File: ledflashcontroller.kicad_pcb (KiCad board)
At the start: 2 copper layers, 100 x 100 mm, 68 parts, among them J1 Conn_02x08_Odd_Even, J2 CONN_01X02, J3 CONN_01X02, K1 LDD-1000H, K2 LDD-1000H, P1 V_DIM1, P10 BNC, P11 BNC, P12 BNC, P2 V_DIM2, P3 V_OUT, P4 V_IN, P5 I2C_HEADER, P6 GPIO_HEADER, P7 BNC, P8 BNC, P9 BNC, Q1 IRLML6244, Q2 IRFB3256, U1 Teensy3.6, U10 DMC2700, U2 ISO1540, U3 DMC2700, U4 DMC2700, U5 ISO1540, U6 DMC2700, U7 DMC2700, U8 ISO1540, U9 DMC2700

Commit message: Fixed some annotations and footprints
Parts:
- removed the P6 at (-56.7, 70.3)
- added P3: GPIO_HEADER, Pin_Headers:Pin_Header_Straight_1x06_Pitch2.54mm, F.Cu at (-40.1, 70.3)
- J1: footprint Pin_Headers:Pin_Header_Straight_2x08_Pitch1.00mm -> Pin_Headers:Pin_Header_Straight_2x08_Pitch2.54mm_SMD
- P10, P11, P12, P7, P8, P9: footprint Connectors_TE-Connectivity:BNC_Socket_TYCO-AMP_LargePads -> lib_fp:BNC_Socket_RSpro_LargePads
- renumbered P4 to P1, P5 to P2, P1 to P4, P2 to P5, P3 to P6, R8 to R1, R14 to R12, R12 to R13, R13 to R14, R17 to R15, R15 to R16, R16 to R17, R9 to R2, R22 to R20, R20 to R21, R21 to R22, R25 to R23, R23 to R24, R24 to R25, R30 to R28, R28 to R29, R7 to R3, R29 to R30, R33 to R31, R31 to R32, R32 to R33, R2 to R4, R3 to R5, R1 to R6, R4 to R7, R6 to R8, R5 to R9
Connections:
- U1 pad 23: (no net) -> /SCK1

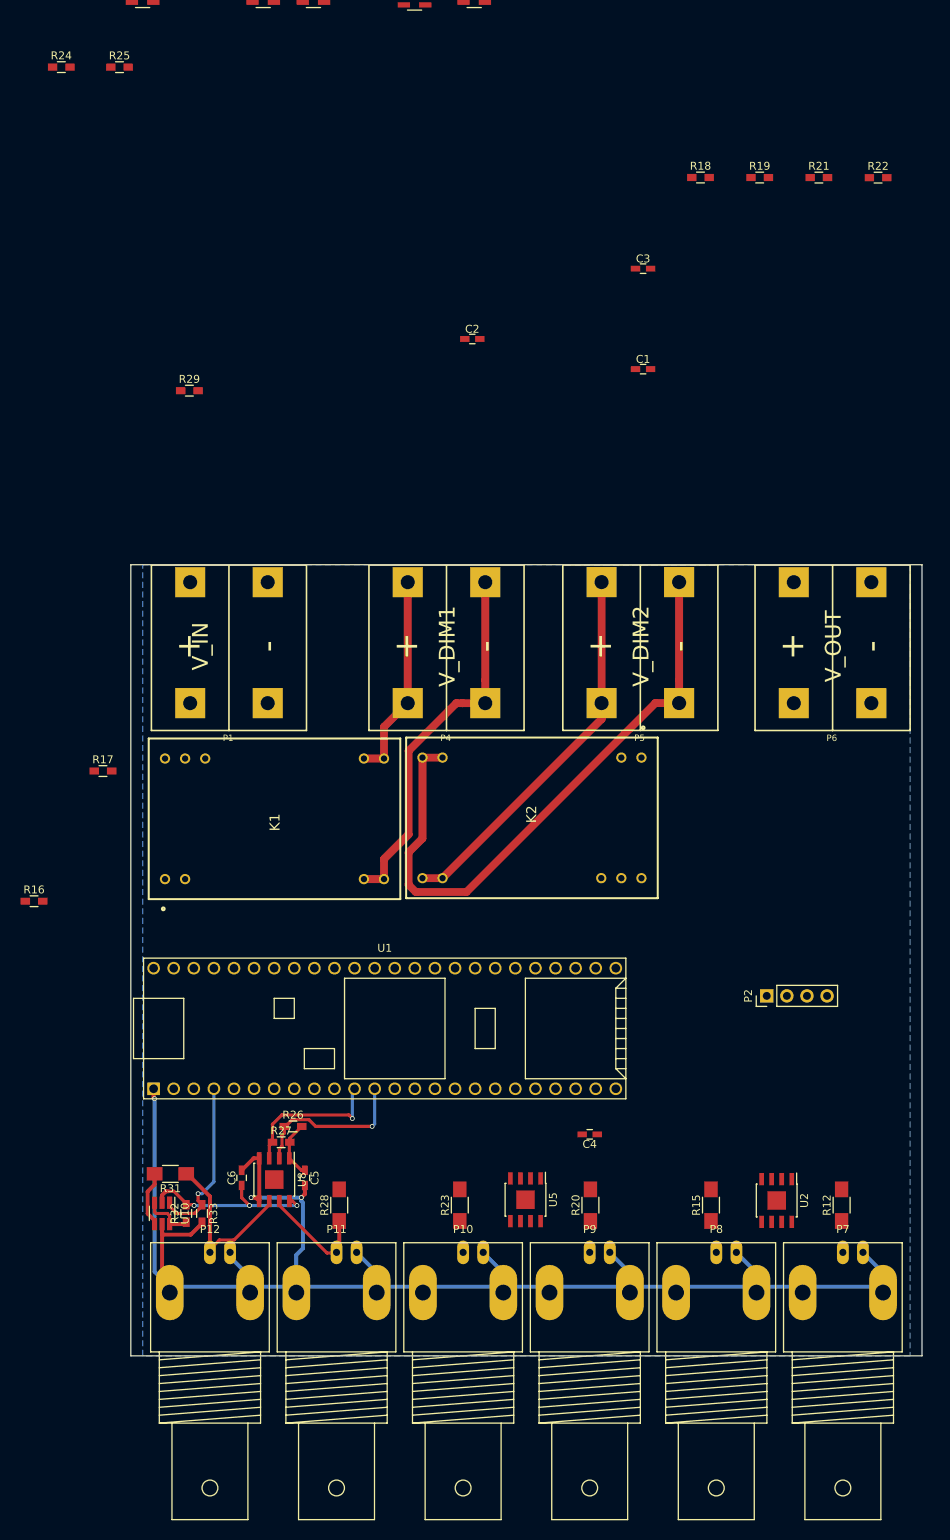
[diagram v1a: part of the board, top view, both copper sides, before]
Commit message: Restructured existing connections and aligned everythink to grid
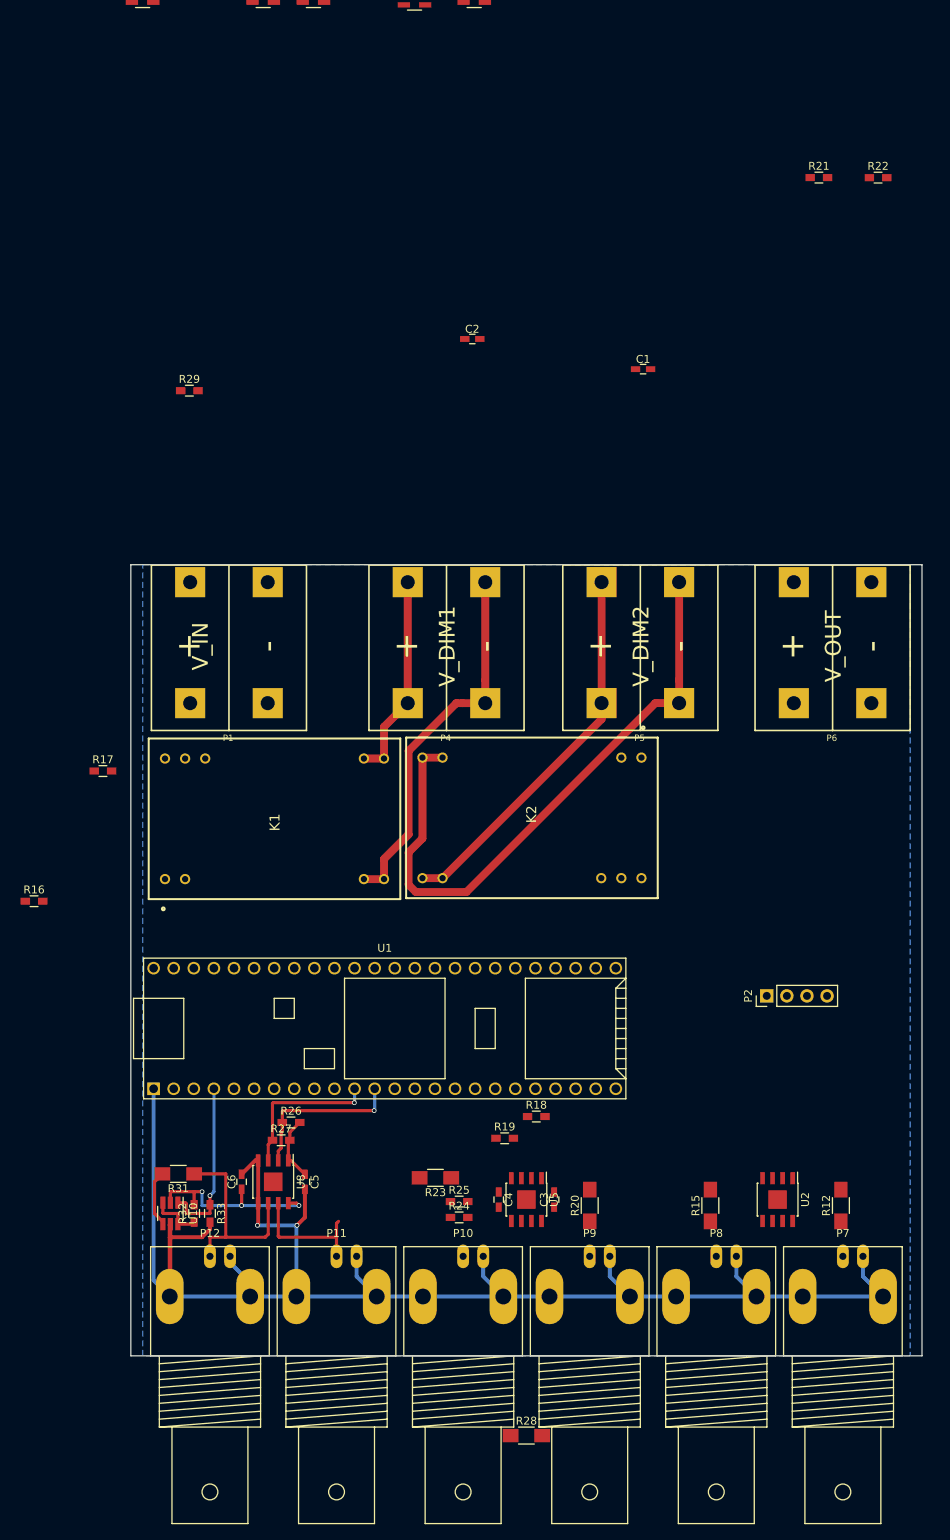
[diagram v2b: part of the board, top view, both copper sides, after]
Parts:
- moved R24 153.8 mm to (71.5, 112.5)
- moved R25 149.7 mm to (71.5, 110.5)
- moved R19 125.6 mm to (77.2, 102.5)
- moved R18 120.5 mm to (81.2, 99.8)
- moved C3 118.2 mm to (83.5, 110.2), turned to 90 degrees
- moved R28 37.5 mm to (80.0, 140.1), turned to 0 degrees
- moved C4 14.2 mm to (76.5, 110.2), turned to 270 degrees
- moved R23 4.62 mm to (68.5, 107.5), turned to 180 degrees
- moved U10 1.05 mm to (35.0, 112.0)
- moved R31 1.00 mm to (36.0, 107.0)
- moved R32 1.00 mm to (38.0, 112.0)
- moved R33 1.00 mm to (40.0, 112.0)
- moved R26 0.56 mm to (50.2, 100.5)
- moved C5 0.50 mm to (52.0, 108.0)
- moved C6 0.50 mm to (44.0, 108.0)
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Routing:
- net GND: track 195.6 -> 209.0 mm, vias 3 -> 2
- net /TrigInOutPu3/TRIG_CON2: track 22.8 -> 25.9 mm
- net /TrigInOutPu3/TRIG_CON1: track 14.5 -> 16.1 mm
- net +5V: track 23.4 -> 24.6 mm

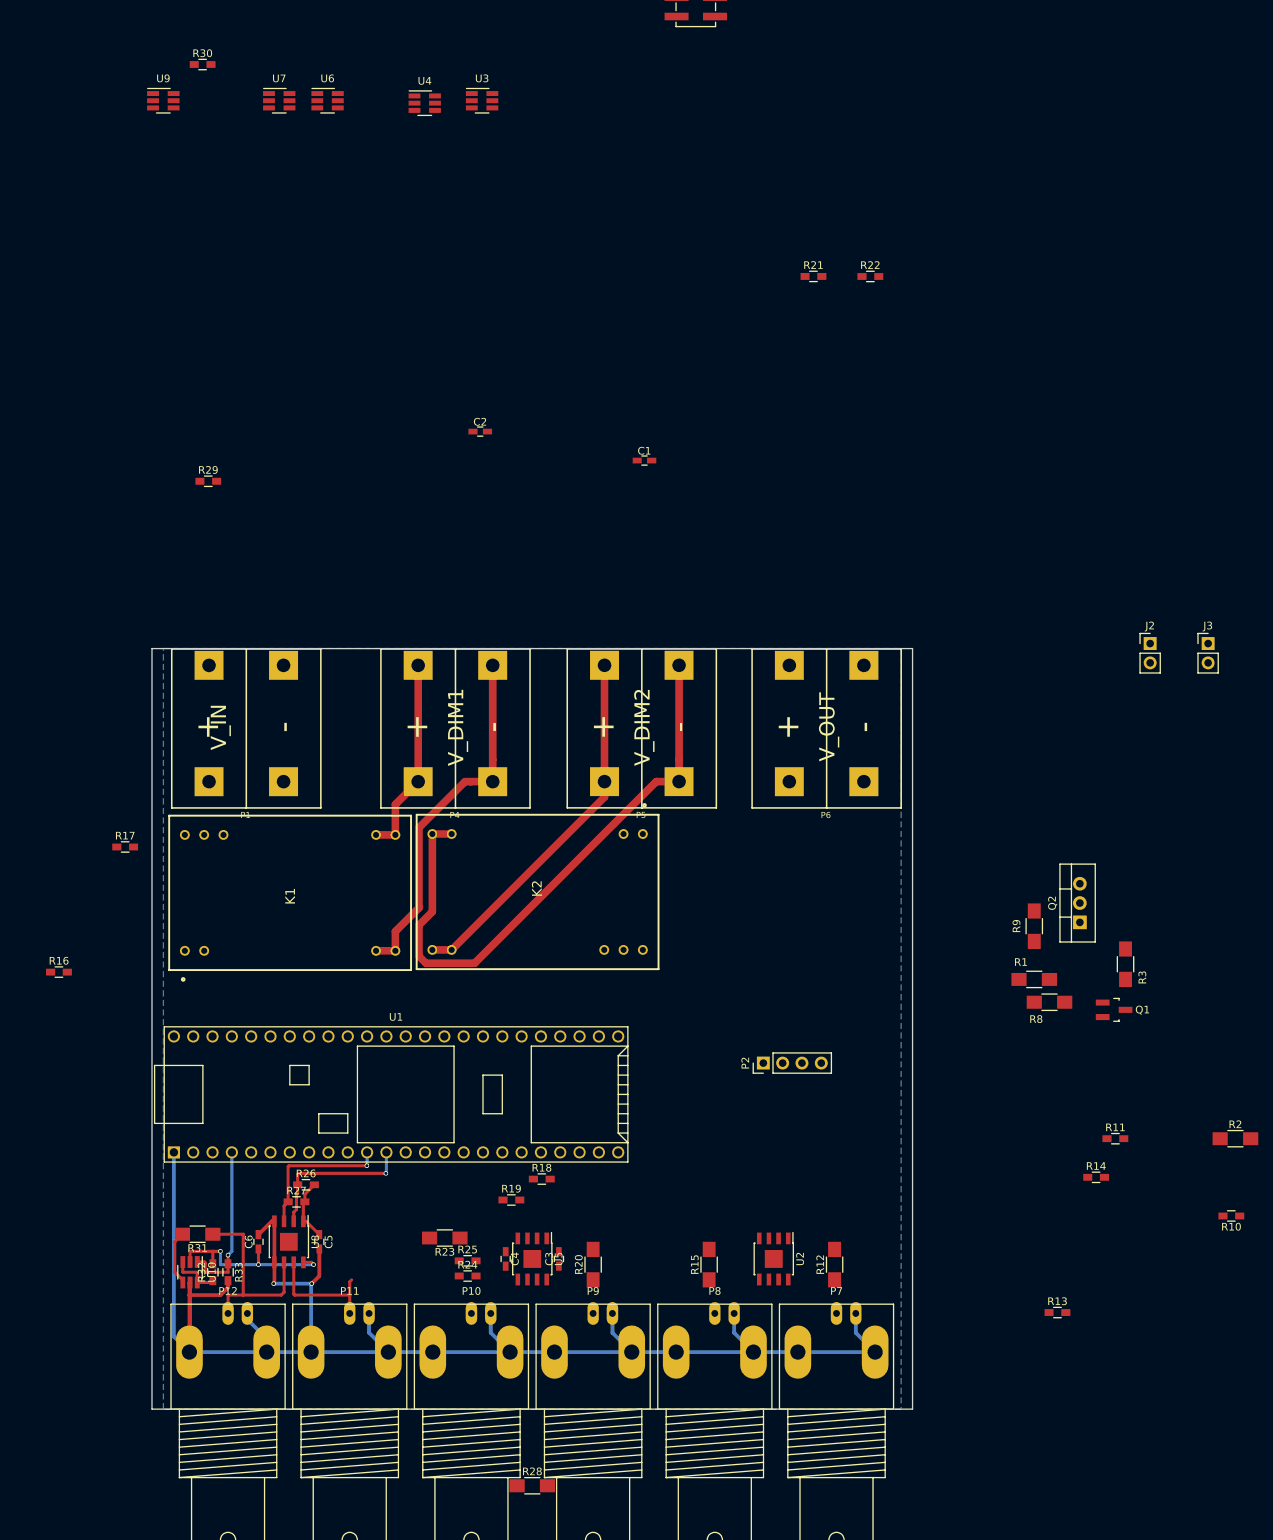
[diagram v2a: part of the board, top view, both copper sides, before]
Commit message: Duplicated existing circuits
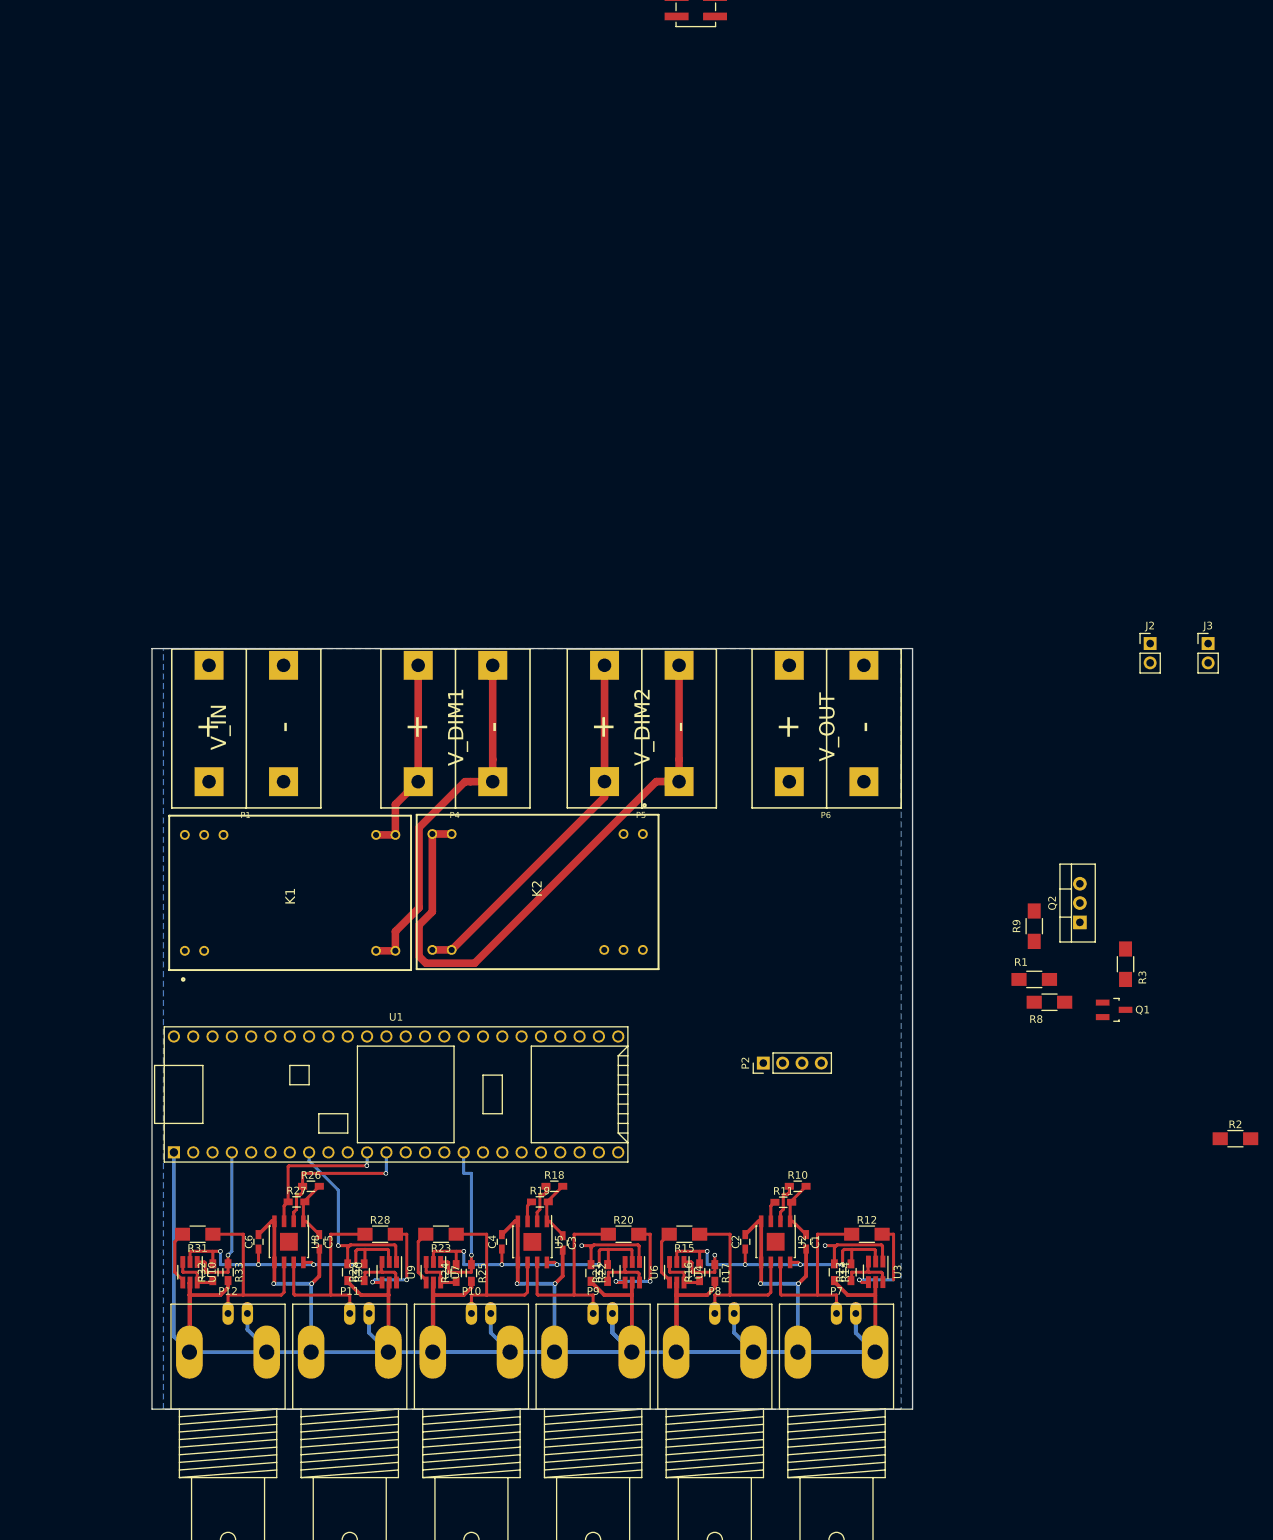
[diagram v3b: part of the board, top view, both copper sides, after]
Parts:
- moved U3 162.4 mm to (125.2, 112.0), turned to 270 degrees
- moved R30 159.9 mm to (55.7, 112.0), turned to 270 degrees
- moved U6 159.2 mm to (93.2, 112.0), turned to 270 degrees
- moved U4 157.2 mm to (99.0, 112.0), turned to 270 degrees
- moved U9 156.9 mm to (61.2, 112.0), turned to 270 degrees
- moved U7 155.4 mm to (67.0, 112.0), turned to 270 degrees
- moved R22 136.1 mm to (87.7, 112.1), turned to 270 degrees
- moved R21 133.8 mm to (89.9, 112.1), turned to 90 degrees
- moved C2 112.1 mm to (108.0, 108.0), turned to 90 degrees
- moved R29 106.0 mm to (57.9, 112.0), turned to 90 degrees
- moved C1 104.9 mm to (116.0, 108.0), turned to 270 degrees
- moved R17 95.6 mm to (104.0, 112.1), turned to 270 degrees
- moved R16 93.0 mm to (102.0, 112.0), turned to 90 degrees
- moved R10 57.1 mm to (114.9, 100.7), turned to 0 degrees
- moved R11 44.5 mm to (113.0, 102.8)
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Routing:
- net GND: track 209.0 -> 432.6 mm, vias 2 -> 6
- net +5V: track 24.6 -> 119.4 mm, vias 3 -> 12
- net /TrigInOutPu2/TRIG_CON1: track 0.00 -> 26.5 mm
- net /TrigInOutPu1/TRIG_CON1: track 0.00 -> 26.5 mm
- net /TRIG_PU4: track 0.00 -> 26.3 mm, vias 0 -> 1
- net /TrigInOutPu2/TRIG_CON2: track 0.00 -> 25.9 mm
- net /TrigInOutPu1/TRIG_CON2: track 0.00 -> 25.9 mm
- net /TRIG_PU5: track 0.00 -> 22.1 mm, vias 0 -> 1
- net +3V3: track 8.22 -> 24.9 mm
- net Net-(R20-Pad2): track 0.00 -> 13.7 mm, vias 0 -> 2
- net Net-(R28-Pad2): track 0.00 -> 13.4 mm, vias 0 -> 2
- net Net-(R12-Pad2): track 0.00 -> 13.3 mm, vias 0 -> 1
- net /TRIG_PU2: track 0.00 -> 12.4 mm, vias 0 -> 1
- net /TRIG_PU0: track 0.00 -> 12.4 mm, vias 0 -> 1
- net /TrigInOutPu3/TRIG_CON1: track 16.1 -> 26.5 mm
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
